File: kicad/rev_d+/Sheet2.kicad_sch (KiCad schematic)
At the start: 214 parts, among them J10 vg_old, J12 JUMPER, J13 JUMPER, J14 JUMPER, J5 JUMPER, J6 JUMPER, J8 JUMPER, J9 JUMPER, Q2 QUARTZ, Q3 QUARTZ32768, X11 KEYB-MOUSE, X12 IDC20, X13 USB_C, X15 PLB2-2, X19 WCH LinkE pgm conn, X21 Turbosound conn, X22 PS2 extra input, X23 SEGA pads, X25 USB_C device, X27 USB_A, X28 RJ45_Hanrun_HR911105A_Horizon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, X29 RS232_9, X3 IDC26LPT, X4 IDC10M, X5 IDC10M, X6 IDC10M

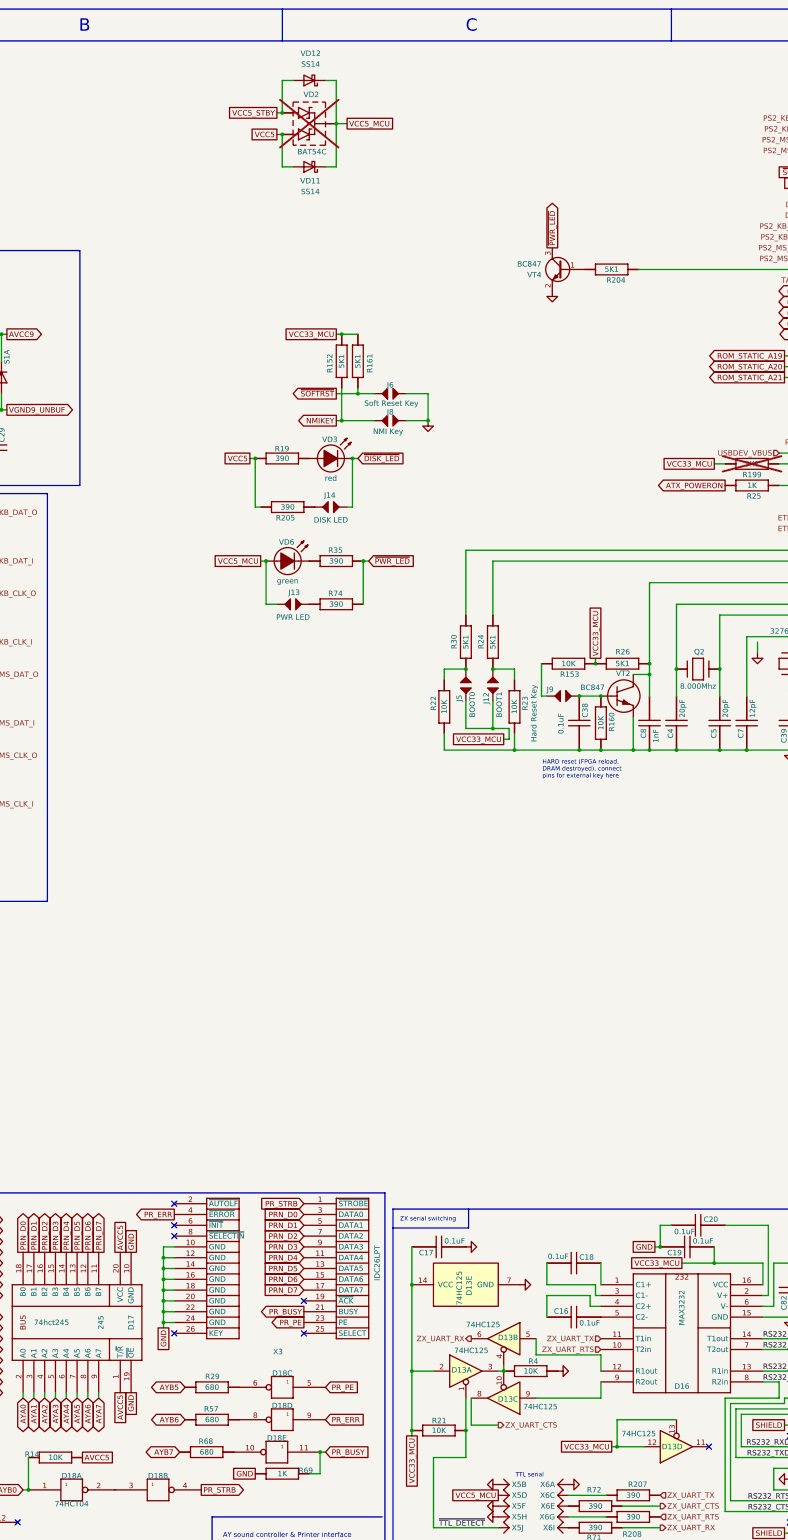
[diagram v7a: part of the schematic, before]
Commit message: pentevo: rev D+: add 5v->3.3v standby, add microSD->LED
git-svn-id: svn://localhost/local-pentevo@1312 c6c76956-fad2-4150-a3a9-ea0a427205ba
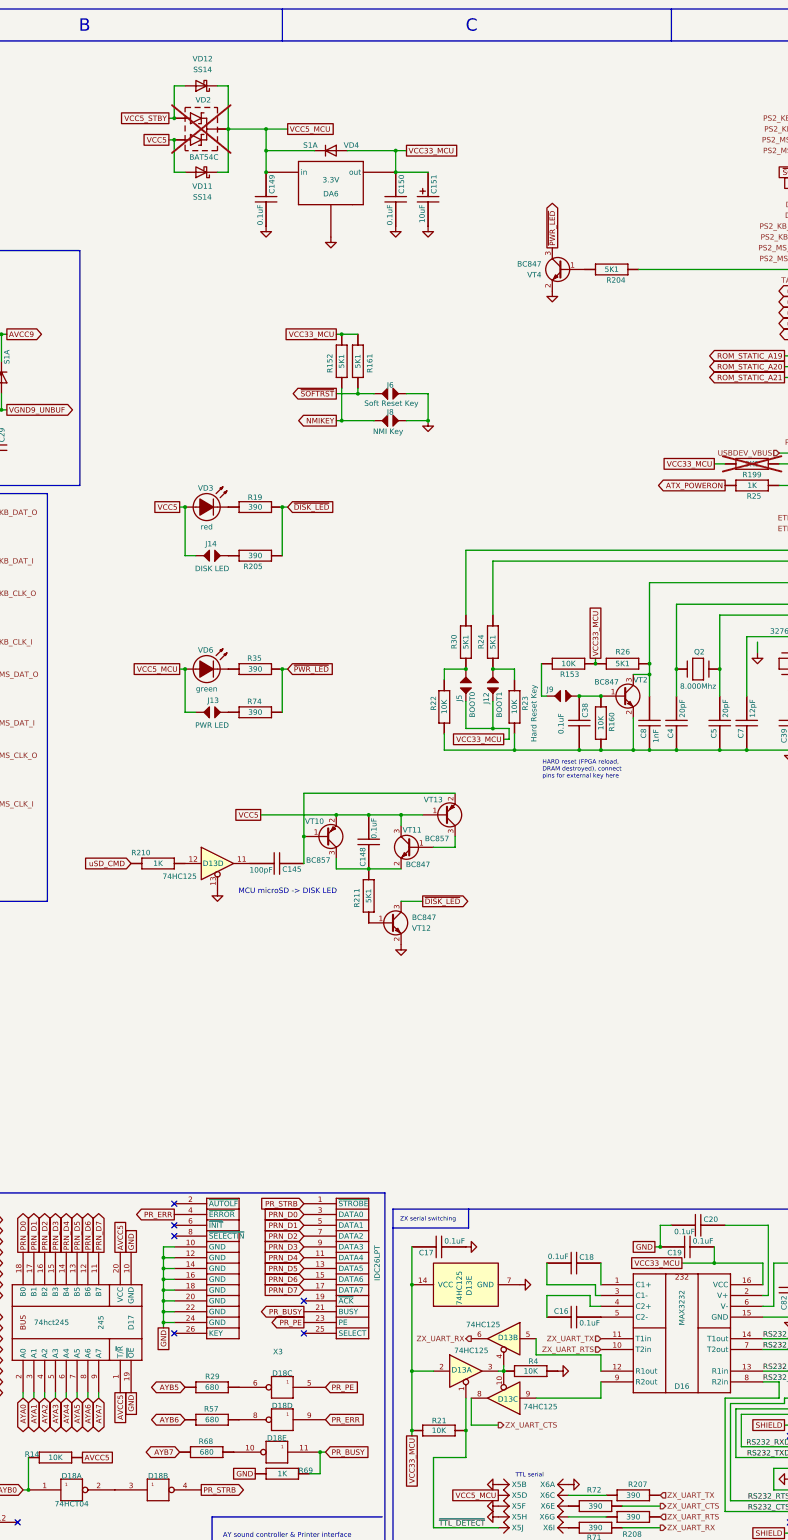
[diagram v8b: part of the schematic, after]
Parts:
- removed VT2: BC847, Package_TO_SOT_SMD:SOT-23_Handsoldering, symbol eva-altium-import:Sheet2_0_BC847
- added C145: 100pF, Capacitor_SMD:C_0805_2012Metric_Pad1.18x1.45mm_HandSolder, symbol eva-altium-import:Sheet2_1_CAPCHIP
- added C148: 0.1uF, C-CHIP, symbol eva-altium-import:Sheet2_2_CAPCHIP
- added C149, C150: 0.1uF, C-CHIP, symbol eva-altium-import:Sheet1_3_CAPCHIP
- added C151: 10uF, EC-CHIP, symbol eva-altium-import:Sheet1_3_ECAPCHIP
- added DA6: 3.3V, DPAK, symbol eva-altium-import:Sheet1_0_NCP1117DT
- added R210: 1K, R-CHIP, symbol eva-altium-import:Sheet2_3_RESCHIP
- added R211: 5K1, R-CHIP, symbol eva-altium-import:Sheet2_0_RESCHIP
- added VD4: S1A, Diode_SMD:D_SMA, symbol Diode:US1A
- added VT10, VT13: BC857, Package_TO_SOT_SMD:SOT-23_Handsoldering, symbol Transistor_BJT:BC857
- added VT11, VT12, VT2: BC847, Package_TO_SOT_SMD:SOT-23_Handsoldering, symbol Transistor_BJT:BC847
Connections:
- net GND: now also D13.13, C149.2, C150.2, C151.2, DA6.1, VT12.2 (E), VT2.2 (E)
- net VCC33_MCU: now also C150.1, C151.1, DA6.2 (out), VD4.2 (A); no longer D13.12, D13.13
- net VCC5: now also J14.1 (2), VD3.A, C148.2, VT10.2 (E), VT11.3 (C), VT13.1 (B); no longer R19.1 (i/o), R205.1 (i/o)
- net VCC5_MCU: now also C149.1, DA6.3 (in), VD4.1 (K)
- net uSD_CMD: now also R210.2 (i/o1)
- net ~{DISK_LED}: now also R19.2 (i/o1), R205.2 (i/o1), VT12.3 (C); no longer J14.0 (1), VD3.K
- net at C8.2, D4.14 (NRST), R26.1 (i/o): now also VT2.3 (C)
- net at C38.1, J9.0 (1), R160.1 (i/o): now also VT2.1 (B)
- net at D13.11: now also C145.2
- new net: R19.1 (i/o), VD3.K
- new net: C148.1, R211.1 (i/o), VT10.3 (C), VT11.2 (E)
- new net: VT11.1 (B), VT13.3 (C)
- new net: J14.0 (1), R205.1 (i/o)
- new net: C145.1, VT10.1 (B), VT13.2 (E)
- new net: D13.12, R210.1 (i/o)
- new net: R211.2 (i/o1), VT12.1 (B)
- no-connect marks 38 -> 37
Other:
- note added: "MCU microSD -> DISK LED"
- moved on the sheet: D13D, J13, R35, R74, VD11, VD12, VD2, VD6
